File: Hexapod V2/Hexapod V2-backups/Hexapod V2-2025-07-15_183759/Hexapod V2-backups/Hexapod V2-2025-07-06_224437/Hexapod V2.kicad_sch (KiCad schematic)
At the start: 38 parts, among them J1 Battery, J2 Switch, U1 MPU6050, U2 NRF24L01_Breakout, U3 ACS712xLCTR-05B, U4 Teensy 4.1

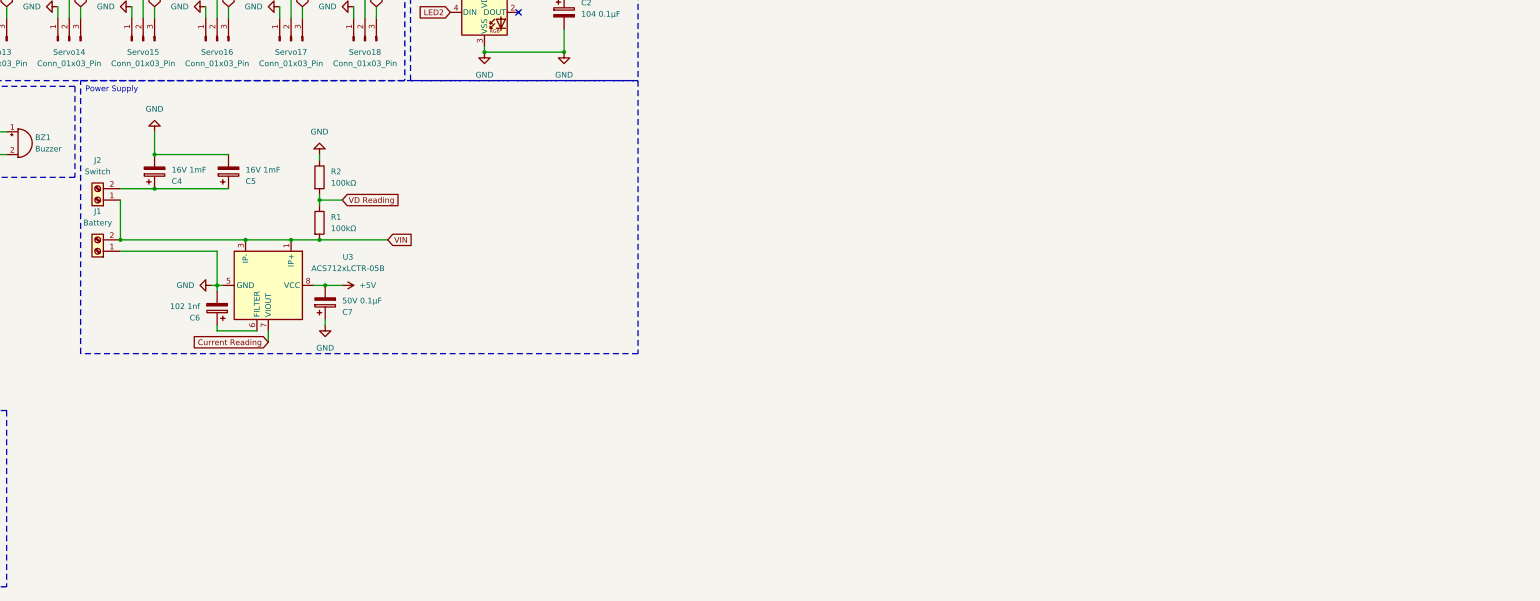
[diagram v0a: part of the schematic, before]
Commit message: Added Teensy
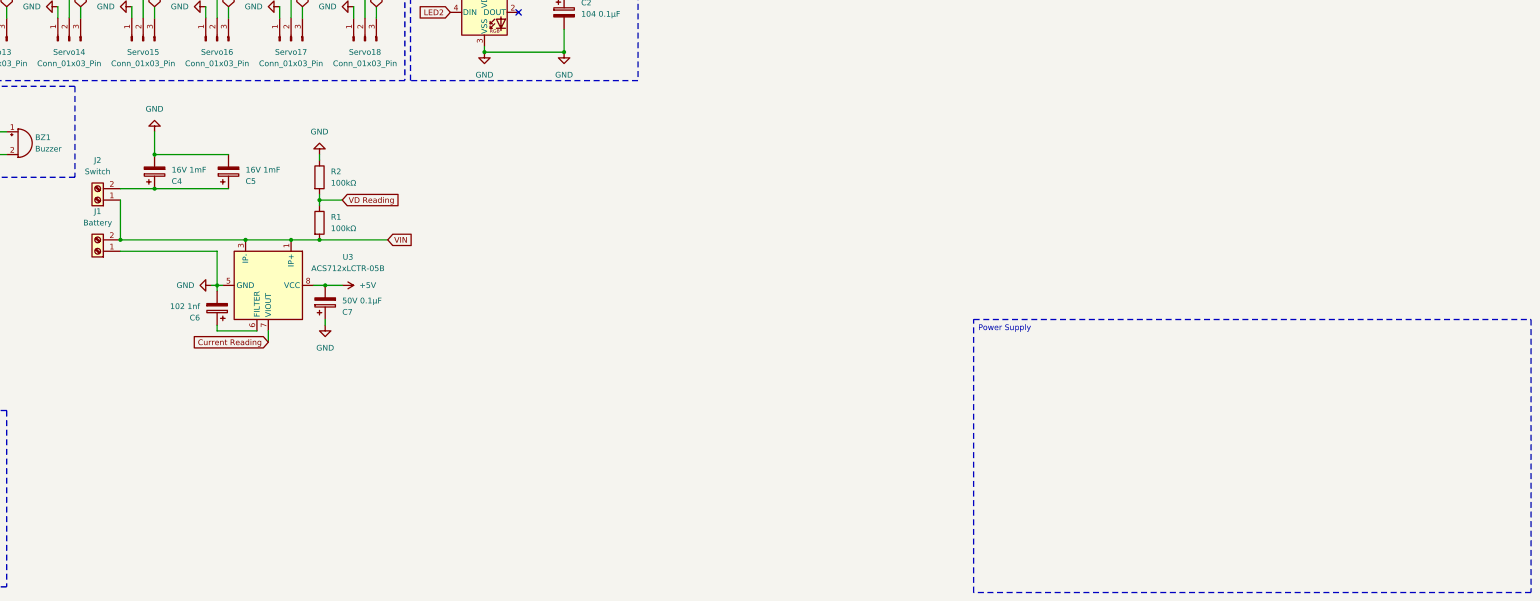
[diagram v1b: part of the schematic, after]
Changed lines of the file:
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@@
 	(text_box "Power Supply"
 		(exclude_from_sim no)
-		(at 158.75 83.82 0)
+		(at 358.14 137.16 0)
 		(size 124.46 60.96)
 		(stroke
